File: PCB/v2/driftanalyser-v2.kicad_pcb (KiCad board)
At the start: 2 copper layers, 110 x 75 mm, 101 parts, among them J1 XT60PW-M, J11 LED1, J12 LED2, J13 LED3, J14 LED4, J15 LED5, J16 LED6, J2 USB-C 16P, J3 UART0, J4 EXT, J5 microSD, J6 OBD, SW1 EN, SW2 BOOT, U1 ESP32-S3-WROOM-1-N16R2, U2 BTS7002-1EPP, U3 AP63200WU-7, U4 AP7361C-33E, U5 LSM6DS3TR-C, U6 USBLC6-2SC6, U7 74HCT245PW, U8 TJA1051T/3, U9 TJA1027T/20

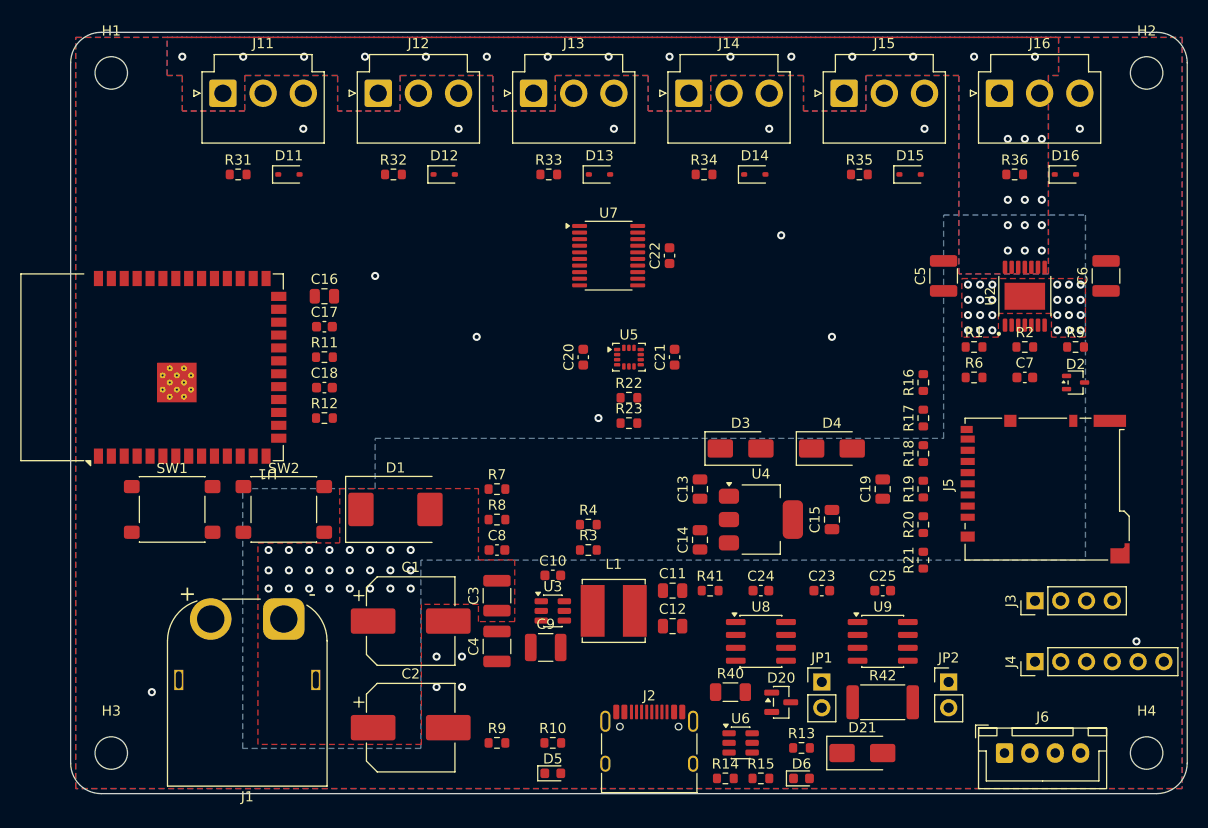
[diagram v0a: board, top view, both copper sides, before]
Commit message: pcb v2: freerouting pass, power stubs and pour keepouts
Claude-Session: https://claude.ai/code/session_015oqRiQH5gUcw5a6jvR5Zdk
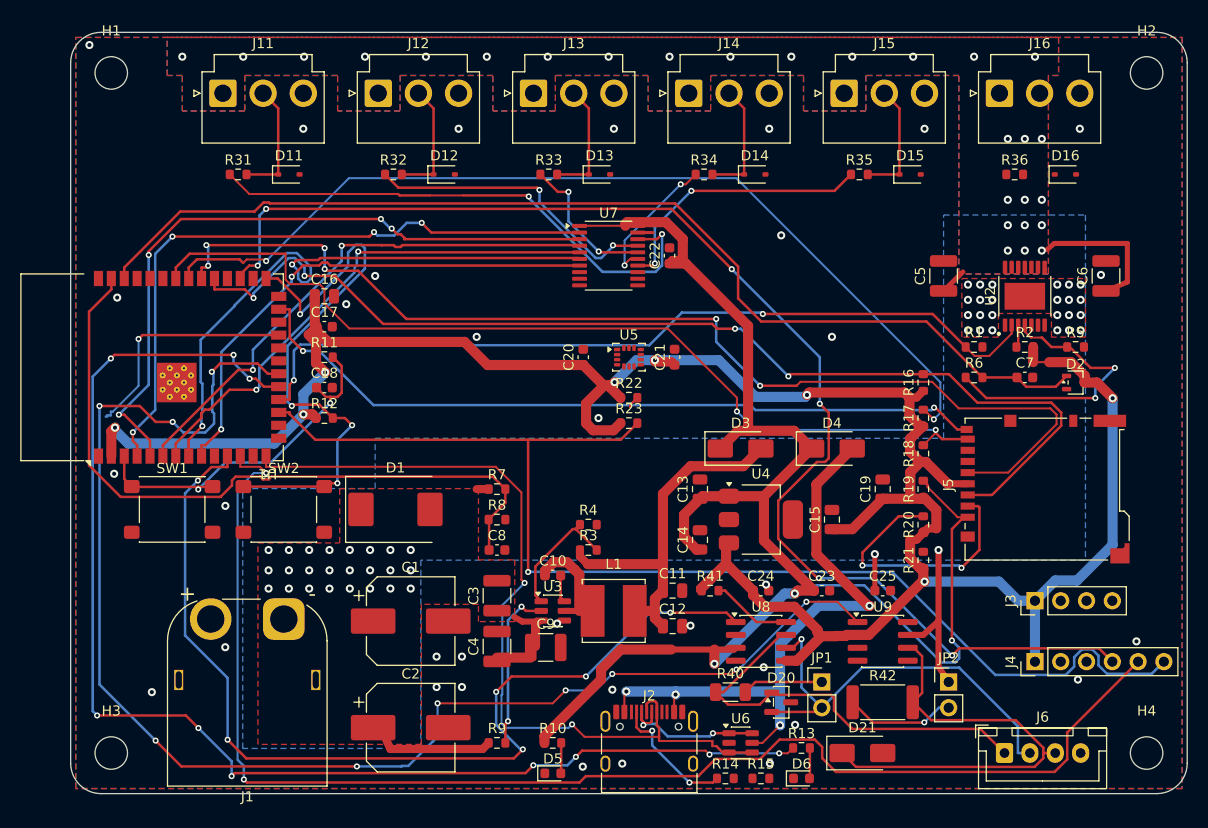
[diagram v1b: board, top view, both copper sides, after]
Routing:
- net 3V3: track 0.00 -> 244.6 mm, vias 0 -> 8
- net K_RX: track 0.00 -> 140.3 mm, vias 0 -> 10
- net I2C_SDA: track 0.00 -> 135.4 mm, vias 0 -> 2
- net UART2_RX: track 0.00 -> 128.3 mm, vias 0 -> 6
- net STATUS_LED: track 0.00 -> 127.9 mm, vias 0 -> 10
- net I2C_SCL: track 0.00 -> 120.7 mm, vias 0 -> 1
- net 5V: track 0.00 -> 115.7 mm, vias 0 -> 2
- net SD_CLK: track 0.00 -> 109.1 mm, vias 0 -> 6
- net SD_CMD: track 0.00 -> 107.1 mm, vias 0 -> 4
- net LED_ISENSE: track 0.00 -> 106.4 mm
- net CAN_TX: track 0.00 -> 96.7 mm, vias 0 -> 6
- net SD_D0: track 0.00 -> 92.9 mm, vias 0 -> 2
- net SD_D1: track 0.00 -> 92.3 mm, vias 0 -> 2
- net USB_DP: track 0.00 -> 83.2 mm, vias 0 -> 2
- net LED_PWR_EN: track 0.00 -> 81.9 mm, vias 0 -> 2
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
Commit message: pcb v2: reroute, power class 0.5, gnd routed not poured, 8 links left
Claude-Session: https://claude.ai/code/session_015oqRiQH5gUcw5a6jvR5Zdk
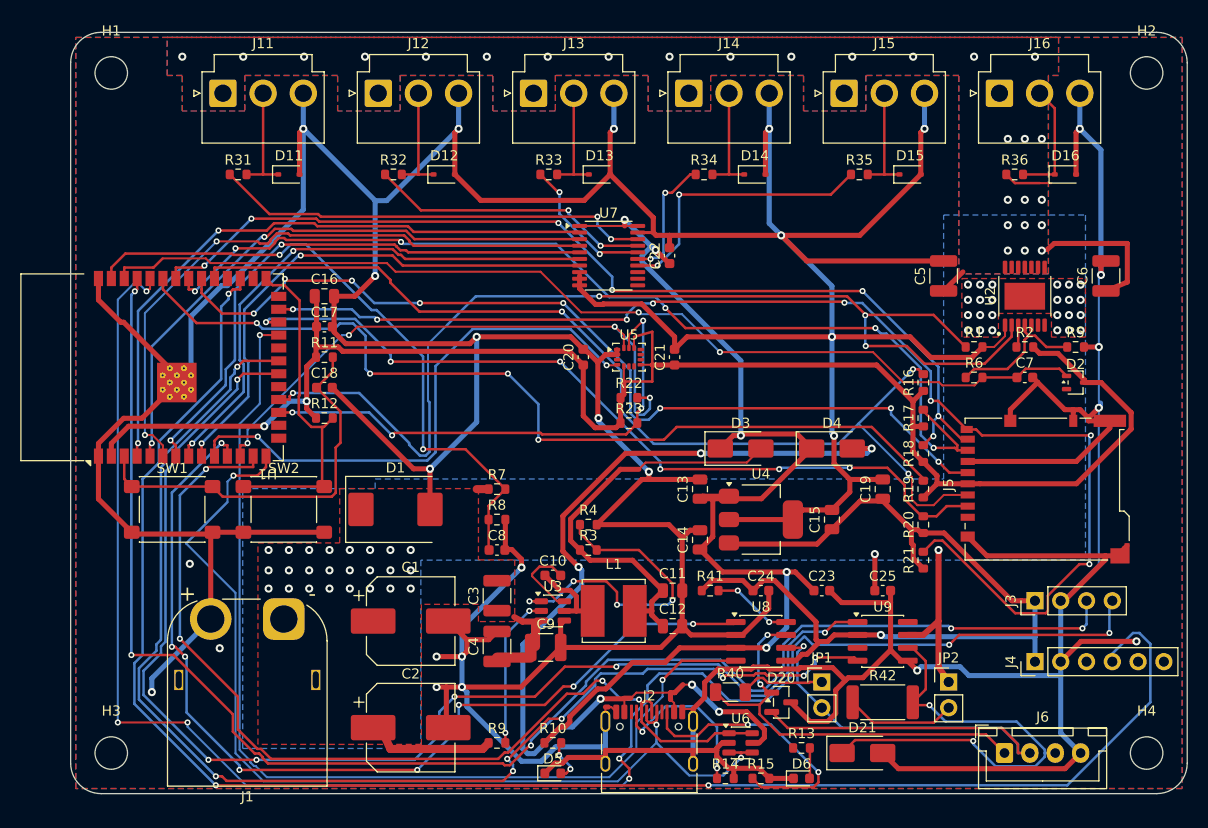
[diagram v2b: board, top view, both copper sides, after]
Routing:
- net GND: track 1.10 -> 837.7 mm, vias 34 -> 27
- net UART0_RX: track 0.00 -> 166.5 mm, vias 0 -> 7
- net UART0_TX: track 0.00 -> 149.8 mm, vias 0 -> 5
- net STATUS_LED: track 127.9 -> 0.00 mm, vias 10 -> 0
- net K_TX: track 0.00 -> 123.6 mm, vias 0 -> 8
- net USB_DN: track 14.6 -> 95.9 mm, vias 2 -> 4
- net CAN_RX: track 23.4 -> 100.9 mm, vias 1 -> 2
- net I2C_SDA: track 135.4 -> 59.2 mm, vias 2 -> 4
- net I2C_SCL: track 120.7 -> 50.3 mm, vias 1 -> 4
- net SD_D3: track 26.5 -> 80.8 mm, vias 2 -> 6
- net IMU_INT1: track 0.00 -> 54.2 mm, vias 0 -> 2
- net SD_D2: track 38.7 -> 89.4 mm, vias 1 -> 4
- net SD_CD: track 74.5 -> 124.0 mm, vias 2 -> 8
- net UART2_RX: track 128.3 -> 165.0 mm, vias 6 -> 3
- net VBUS_USB: track 60.4 -> 95.5 mm, vias 4 -> 6
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
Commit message: pcb v2: headers next to the esp, split vbat corridor, 4 links left
Claude-Session: https://claude.ai/code/session_015oqRiQH5gUcw5a6jvR5Zdk
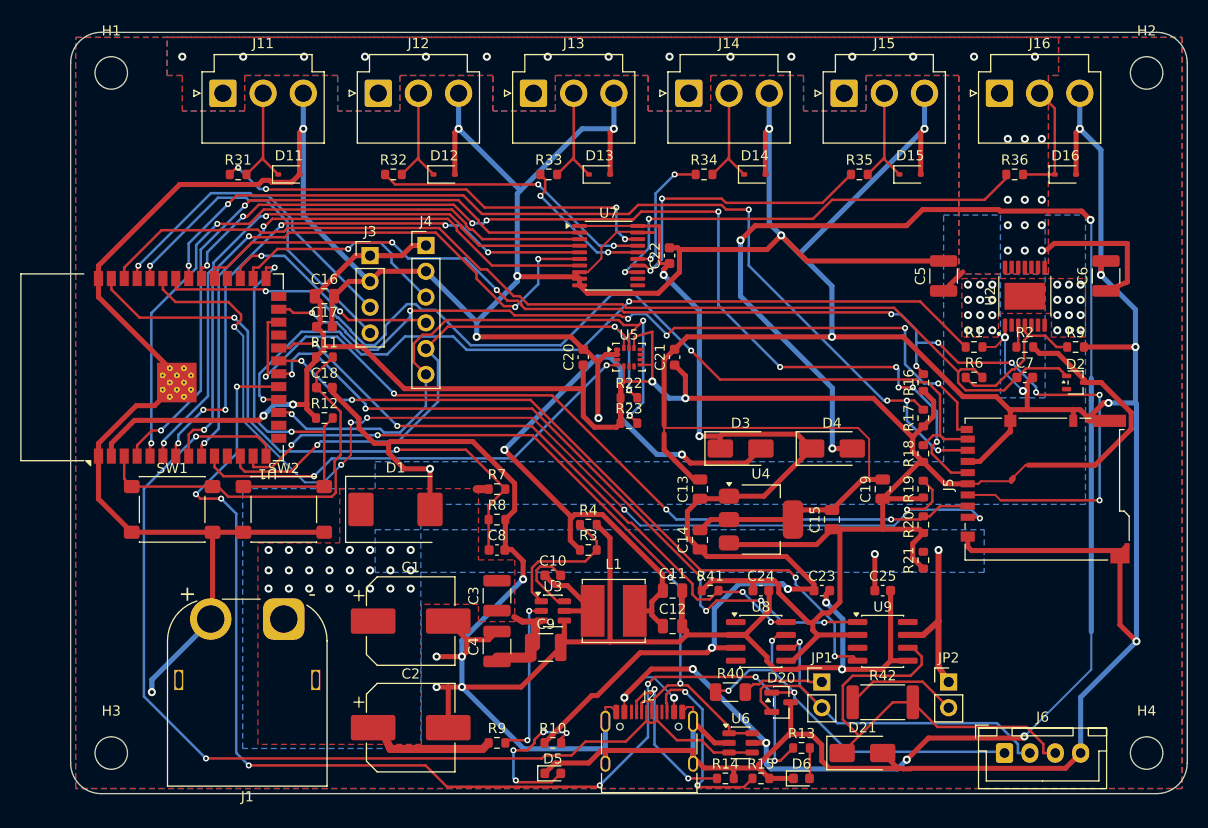
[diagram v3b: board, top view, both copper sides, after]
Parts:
- moved J3 73.8 mm to (29.5, 22.0), turned to 0 degrees
- moved J4 72.7 mm to (35.0, 21.0), turned to 0 degrees
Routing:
- net UART2_RX: track 165.0 -> 22.6 mm, vias 3 -> 2
- net UART0_RX: track 166.5 -> 32.9 mm, vias 7 -> 1
- net UART0_TX: track 149.8 -> 32.3 mm, vias 5 -> 1
- net STATUS_LED: track 0.00 -> 116.2 mm, vias 0 -> 8
- net CAN_RX: track 100.9 -> 0.00 mm, vias 2 -> 0
- net CAN_TX: track 95.2 -> 0.00 mm, vias 8 -> 0
- net VBUS_USB: track 95.5 -> 174.1 mm, vias 6 -> 9
- net CAN_STB: track 7.93 -> 63.0 mm, vias 2 -> 4
- net K_TX: track 123.6 -> 71.6 mm, vias 8 -> 4
- net K_RX: track 123.3 -> 72.4 mm
- net SD_CD: track 124.0 -> 81.0 mm, vias 8 -> 6
- net LED6_OUT: track 4.80 -> 44.7 mm, vias 0 -> 2
- net 5V_BUCK: track 41.0 -> 69.1 mm, vias 0 -> 2
- net LED_PWR_EN: track 106.2 -> 81.6 mm, vias 4 -> 2
- net SD_CMD: track 99.6 -> 123.6 mm, vias 3 -> 9
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
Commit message: pcb v2: 4-layer variant, routed clean
Claude-Session: https://claude.ai/code/session_015oqRiQH5gUcw5a6jvR5Zdk
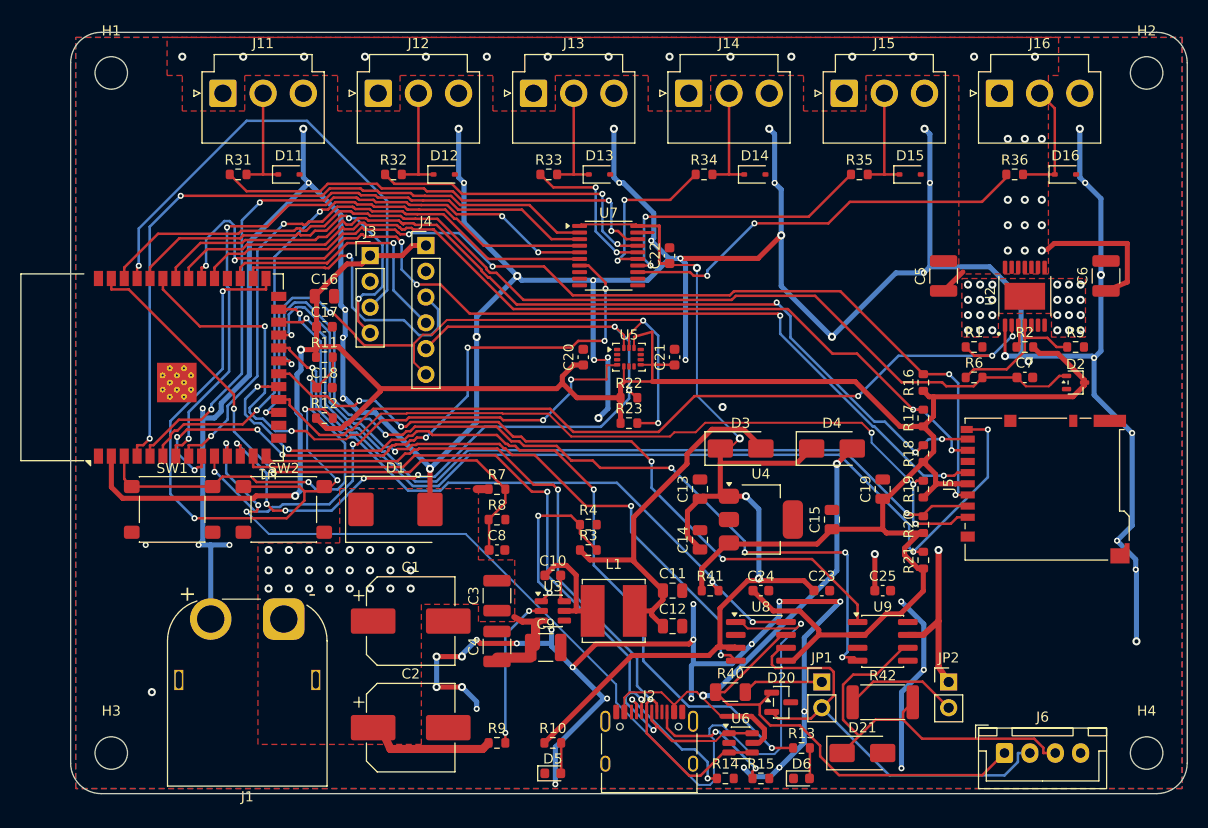
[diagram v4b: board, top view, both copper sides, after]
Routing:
- net GND: track 848.9 -> 458.3 mm, vias 26 -> 65
- net VBUS_USB: track 174.1 -> 52.1 mm, vias 9 -> 2
- net CAN_TX: track 0.00 -> 102.7 mm, vias 0 -> 4
- net CAN_RX: track 0.00 -> 70.2 mm, vias 0 -> 4
- net STATUS_LED: track 116.2 -> 81.5 mm, vias 8 -> 4
- net 5V_BUCK: track 69.1 -> 37.8 mm, vias 2 -> 0
- net USB_DP: track 103.2 -> 73.8 mm
- net SD_CMD: track 123.6 -> 95.1 mm, vias 9 -> 4
- net BOOT: track 40.1 -> 64.7 mm, vias 2 -> 4
- net I2C_SDA: track 59.1 -> 80.0 mm, vias 3 -> 7
- net K_TX: track 71.6 -> 90.3 mm, vias 4 -> 6
- net SD_CD: track 81.0 -> 98.6 mm, vias 6 -> 3
- net UART0_TX: track 32.3 -> 48.3 mm
- net PWR_LED_A: track 15.3 -> 3.02 mm, vias 4 -> 0
- net I2C_SCL: track 61.1 -> 70.5 mm, vias 3 -> 4
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- added copper zone on In2.Cu, net 12V_LED
- added copper zone on In1.Cu, net GND
- added copper zone on In2.Cu, net GND
- added copper zone on In2.Cu, net VBAT
- removed copper zone on B.Cu, net 12V_LED
- removed copper zone on B.Cu, net VBAT
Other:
- copper layers 2 -> 4

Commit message: pcb v2 4-layer: vbat on the whole lower plane, 1 oz inner, replay the ses
Claude-Session: https://claude.ai/code/session_015oqRiQH5gUcw5a6jvR5Zdk
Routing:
- net VBAT: vias 50 -> 114
- net GND: vias 65 -> 66

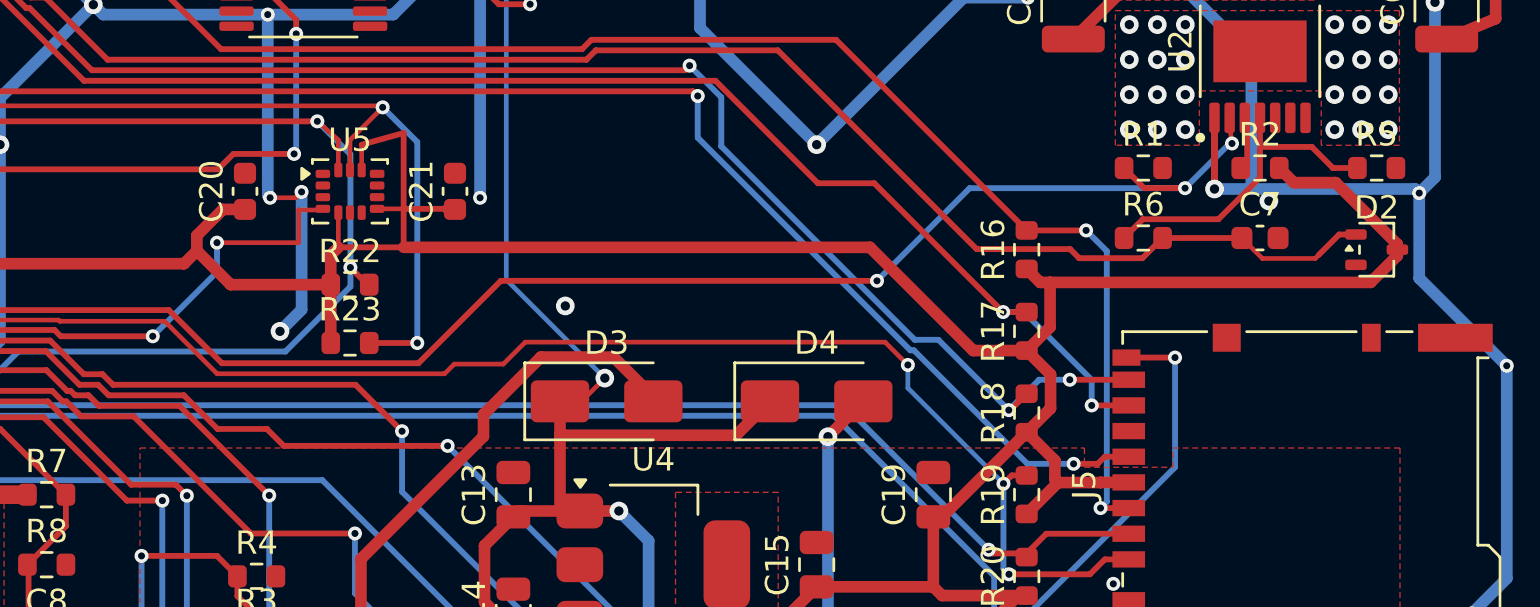
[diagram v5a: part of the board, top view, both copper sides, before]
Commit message: pcb v2 4-layer: fix the riser cross section, scan it transversely, untrack the dsn
Claude-Session: https://claude.ai/code/session_015oqRiQH5gUcw5a6jvR5Zdk
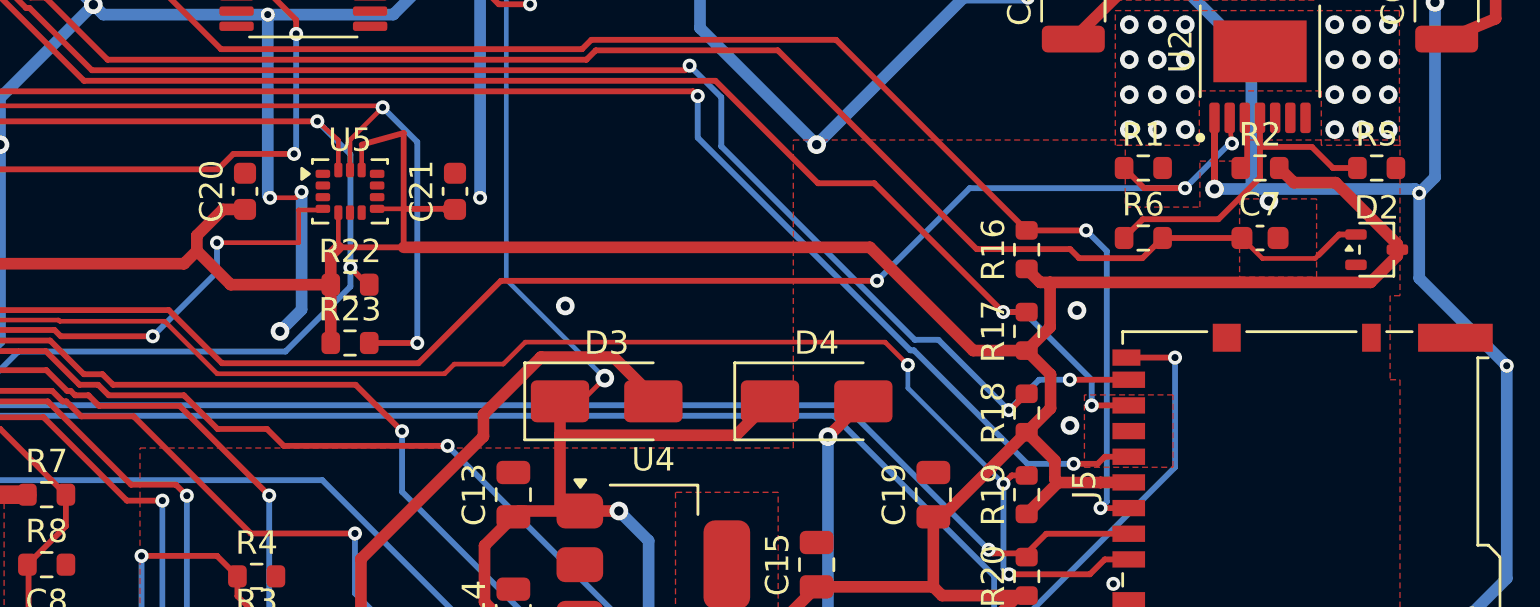
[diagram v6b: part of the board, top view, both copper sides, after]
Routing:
- net GND: vias 66 -> 68
